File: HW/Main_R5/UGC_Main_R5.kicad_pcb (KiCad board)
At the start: 4 copper layers, 125.7 x 76.4 mm, 163 parts, among them J1 SM02B-SURS-TF_LF__SN_, J10 SM02B-SURS-TF_LF__SN_, J13 503480-0640, J2 503480-0640, J4 Conn_01x06_Pin, J5 UJ31-CH-G1-SMT-TR, J6 Trigger, J7 Trigger, J8 Conn_01x02, J9 Conn_01x02, P1 RPI-RM2, Q3 BSS138DW, Q4 BSS138DW, Q5 MMBT2222A, Q6 MMBT2222A, SW1 SW_Push, SW10 SW_Push, SW11 SW_Push, SW12 SW_Push, SW13 SW_Push, SW14 TS-1187A-C-A-B, SW15 1TS026A-1000-0550, SW17 TS-1187A-C-A-B, SW18 TS-1187A-C-A-B, SW19 TS-1187A-C-A-B, SW2 SW_Push, SW3 SW_Push, SW4 SW_Push, SW5 TS-1187A-C-A-B, SW6 GL18_SW, SW7 SW_Push, SW8 SW_Push, SW9 TS-1187A-C-A-B, U1 USBLC6-2P6, U10 ST_LSM6, U11 BQ25180, U2 USBLC6-2P6, U3 USBLC6-2P6, U4 TPS630001RCR, U5 ST_LSM6, U8 RP2040, U9 GD25Q80EEIGR, X1 ModConnect, X2 ModConnect, X3 ModConnect, X4 ModConnect, X5 ModConnect, X6 ModConnect, Y1 ABM8-272-T3

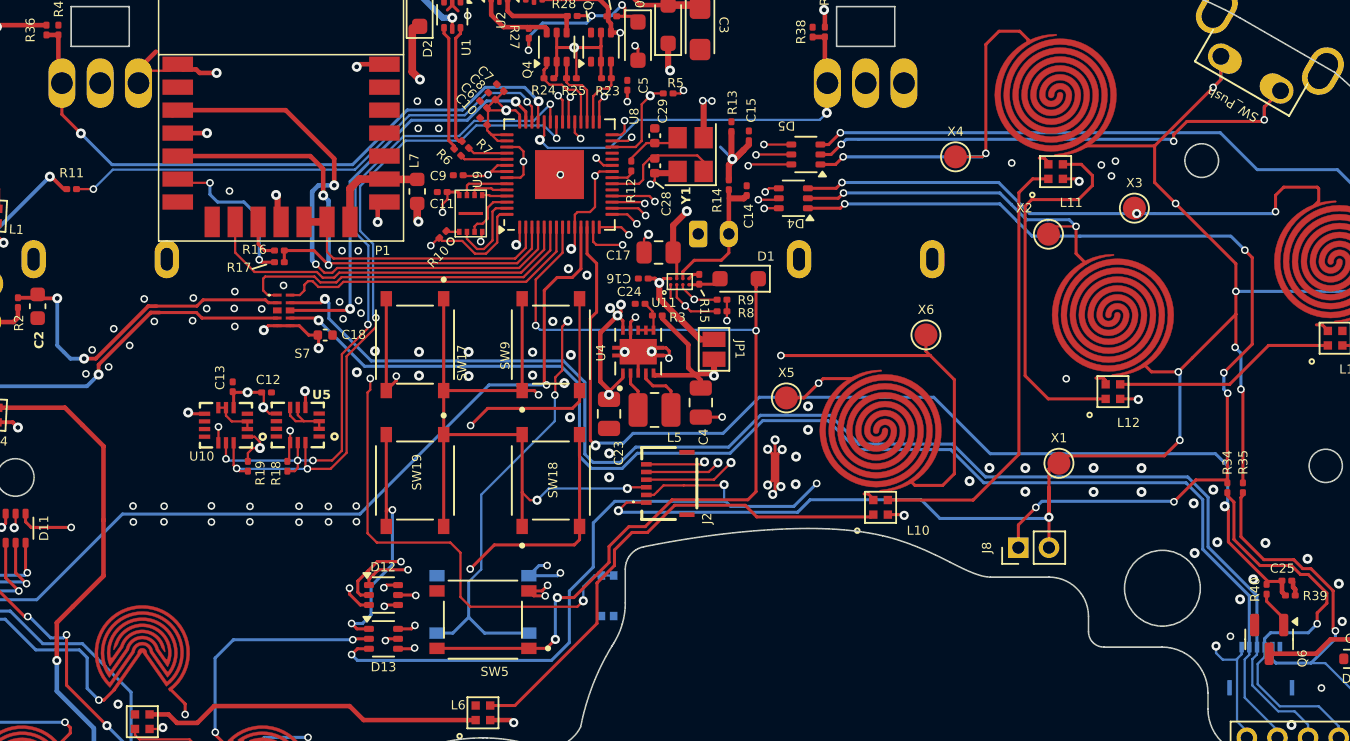
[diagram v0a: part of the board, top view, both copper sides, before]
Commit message: Add BATLVL
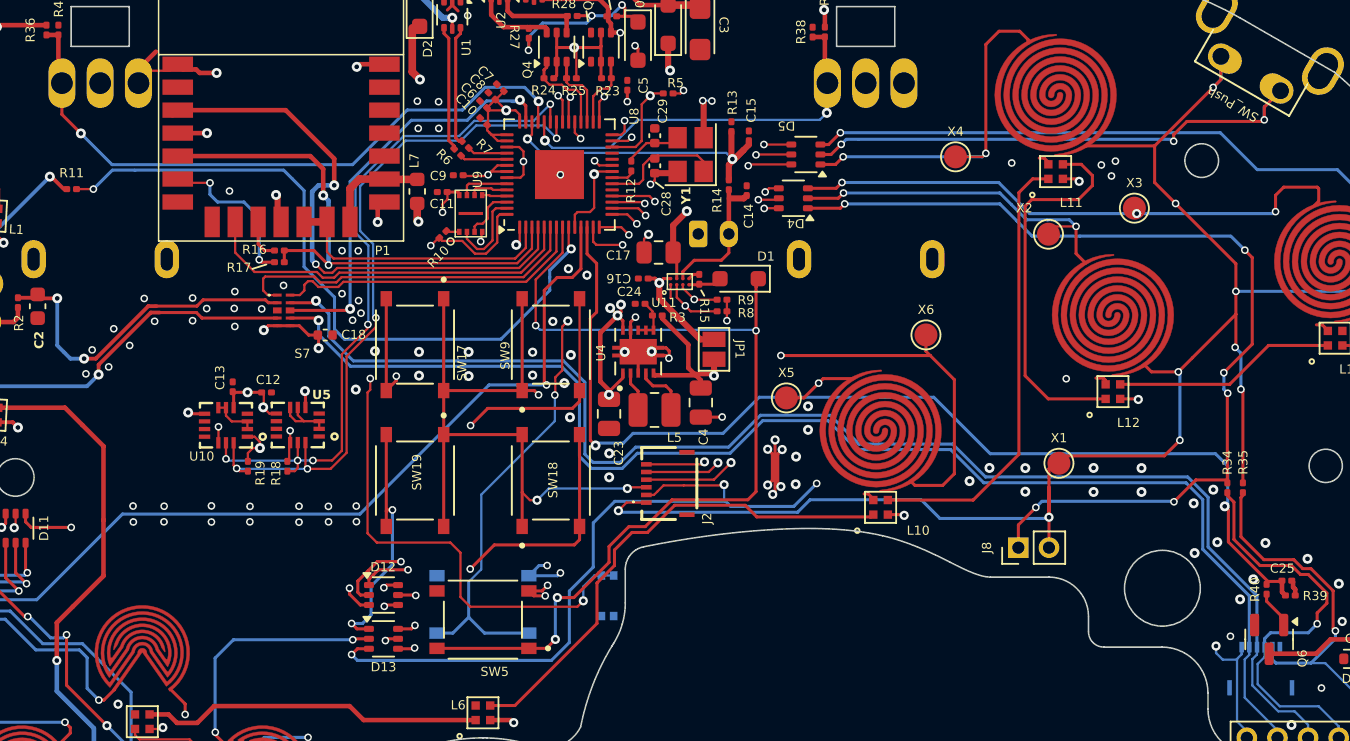
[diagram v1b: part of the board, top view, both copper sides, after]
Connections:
- U8 pad 40: RGB_OUT -> BAT_LVL
- U8 pad 9: unconnected-(U8-GPIO7-Pad9) -> RGB_OUT
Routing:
- net BAT_LVL: track 7.08 -> 21.1 mm, vias 1 -> 2
- net RGB_OUT: track 33.6 -> 46.0 mm
- net +3V3: track 135.3 -> 133.9 mm, vias 55 -> 54
- net ADC_MUX_OUT: track 27.1 -> 27.7 mm
- net RX: track 88.2 -> 88.7 mm
